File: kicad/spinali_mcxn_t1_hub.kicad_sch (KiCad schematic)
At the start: 0 parts

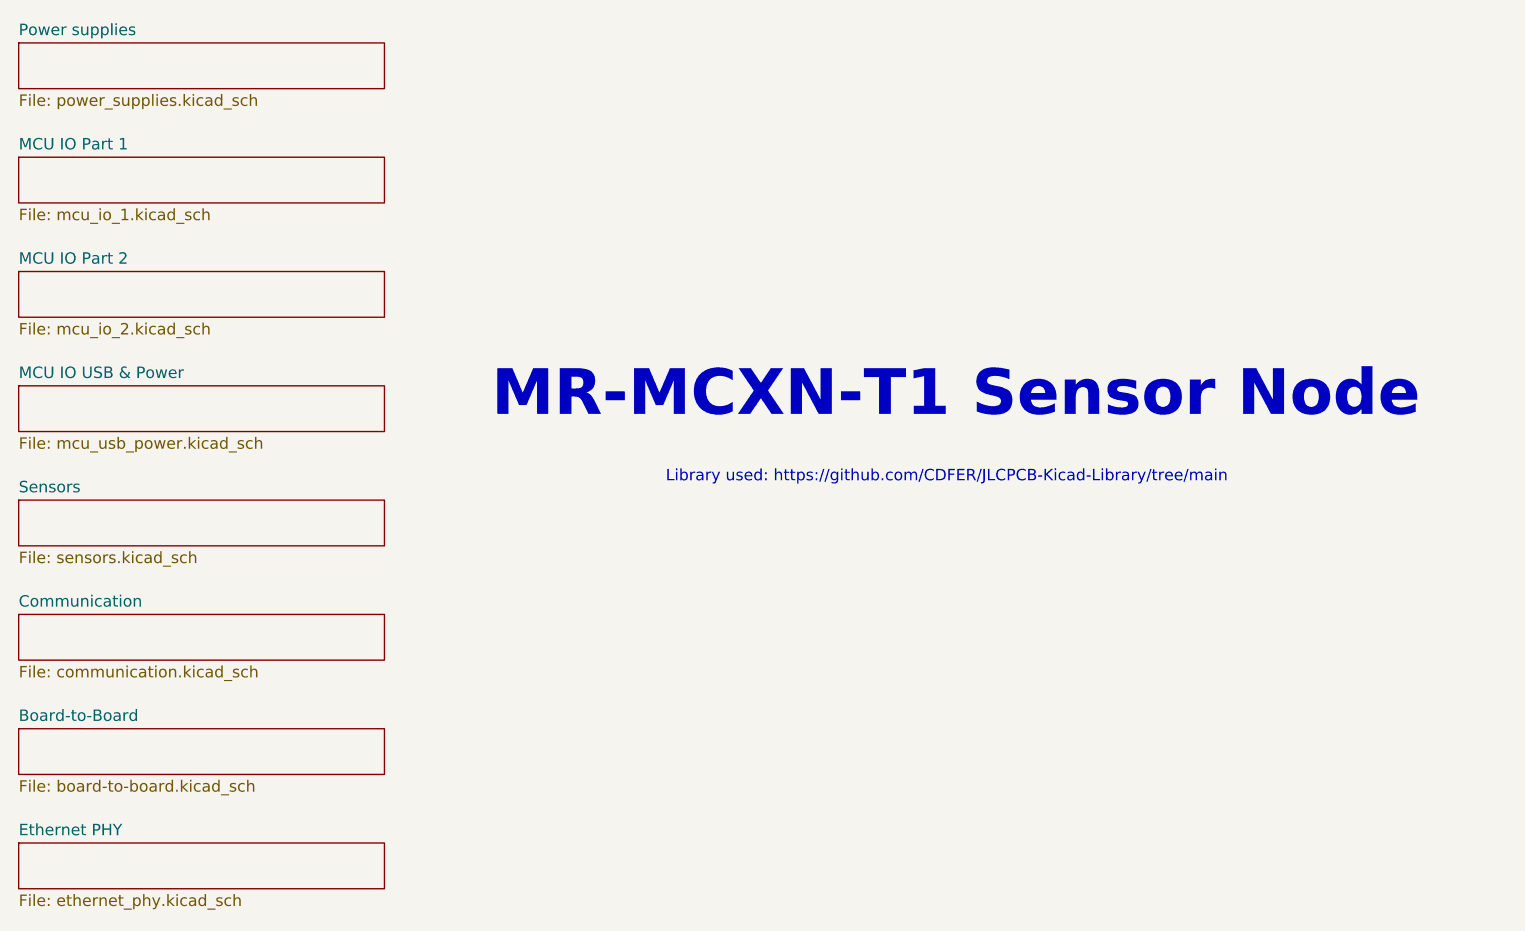
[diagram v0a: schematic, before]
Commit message: Update repo naming and cleanup files.
Signed-off-by: Benjamin Perseghetti <bperseghetti@rudislabs.com>
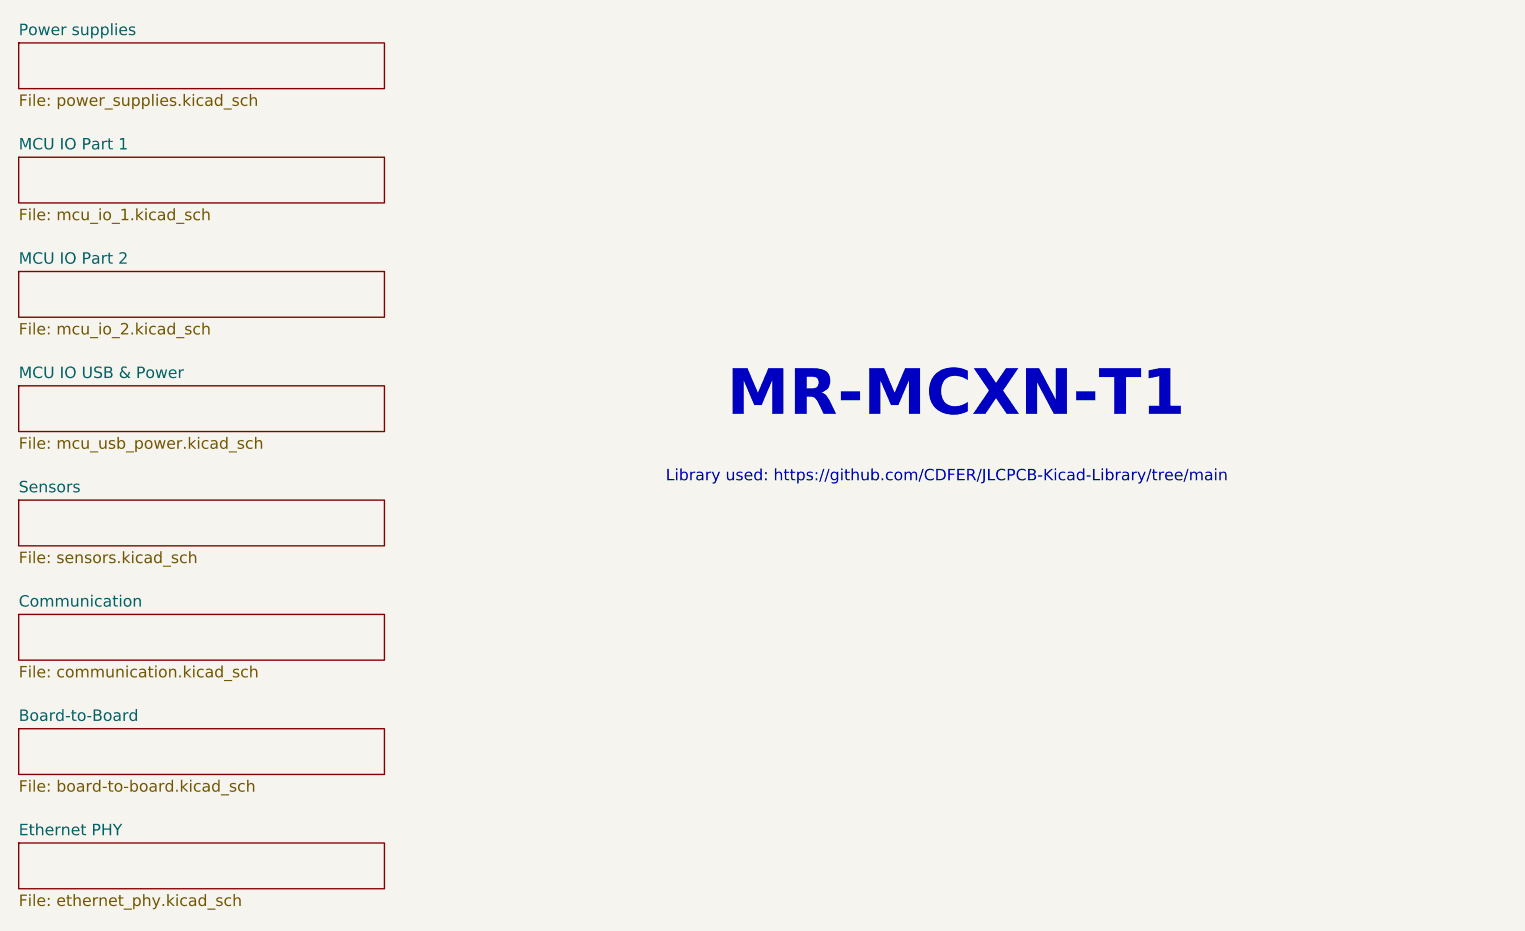
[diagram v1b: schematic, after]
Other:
- note added: "MR-MCXN-T1"
- note removed: "MR-MCXN-T1 Sensor Node"
- title: MR-MCXN-T1 Sensor Node -> MR-MCXN-T1
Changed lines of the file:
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@@
 	(paper "A4")
 	(title_block
-		(title "MR-MCXN-T1 Sensor Node")
+		(title "MR-MCXN-T1")
 		(date "2025-03-28")
 		(rev "X0")
 		(company "NXP SEMICONDUCTORS B.V.")
-		(comment 1 "CLASSIFICATION: INTERNAL USE ONLY")
 		(comment 3 "DESIGNER: YOURI TILS")
 		(comment 4 "CTO SYSTEM INNOVATIONS / MOBILE ROBOTICS DOMAIN")
 	)
-	(text "MR-MCXN-T1 Sensor Node"
+	(text "MR-MCXN-T1"
 		(exclude_from_sim no)
 		(at 154.94 91.186 0)
@@
 		)
 		(instances
-			(project "spinali_mcxn_t1_sensor_hub"
+			(project "spinali_mcxn_t1_hub"
 				(path "/8b469ec1-e800-4d46-8a32-95d77ceae6db"
 					(page "8")
@@
 		)
 		(instances
-			(project "spinali_mcxn_t1_sensor_hub"
+			(project "spinali_mcxn_t1_hub"
 				(path "/8b469ec1-e800-4d46-8a32-95d77ceae6db"
 					(page "3")
@@
 		)
 		(instances
-			(project "spinali_mcxn_t1_sensor_hub"
+			(project "spinali_mcxn_t1_hub"
 				(path "/8b469ec1-e800-4d46-8a32-95d77ceae6db"
 					(page "4")
@@
 		)
 		(instances
-			(project "spinali_mcxn_t1_sensor_hub"
+			(project "spinali_mcxn_t1_hub"
 				(path "/8b469ec1-e800-4d46-8a32-95d77ceae6db"
 					(page "9")
@@
 		)
 		(instances
-			(project "spinali_mcxn_t1_sensor_hub"
+			(project "spinali_mcxn_t1_hub"
 				(path "/8b469ec1-e800-4d46-8a32-95d77ceae6db"
 					(page "6")
@@
 		)
 		(instances
-			(project "spinali_mcxn_t1_sensor_hub"
+			(project "spinali_mcxn_t1_hub"
 				(path "/8b469ec1-e800-4d46-8a32-95d77ceae6db"
 					(page "7")
@@
 		)
 		(instances
-			(project "spinali_mcxn_t1_sensor_hub"
+			(project "spinali_mcxn_t1_hub"
 				(path "/8b469ec1-e800-4d46-8a32-95d77ceae6db"
 					(page "5")
@@
 		)
 		(instances
-			(project "spinali_mcxn_t1_sensor_hub"
+			(project "spinali_mcxn_t1_hub"
 				(path "/8b469ec1-e800-4d46-8a32-95d77ceae6db"
 					(page "2")
